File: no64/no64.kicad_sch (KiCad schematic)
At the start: 15 parts, among them J1 Analog Stick, SW10 Cup, SW11 Cright, SW12 Cdown, SW13 L, SW14 R, SW2 A, SW3 B, SW4 Dleft, SW5 Dup, SW6 Dright, SW7 Ddown, SW8 START, SW9 Cleft, U1 Pico

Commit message: More WIP
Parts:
- added C18: 10u, PhobGCC_2_0_0_footprints:C_0805_2012Metric, symbol Device:C
- added D1: D_Schottky, symbol Device:D_Schottky
- added J2: Conn_01x04_Socket, Connector_PinHeader_2.00mm:PinHeader_1x04_P2.00mm_Vertical, symbol Connector:Conn_01x04_Socket
- added P1: USB_C_Plug_USB2.0, symbol Connector:USB_C_Plug_USB2.0
- added U2: AMS1117-3.3, Package_TO_SOT_SMD:SOT-223-3_TabPin2, symbol Regulator_Linear:AMS1117-3.3
- J1: footprint (none) -> Connector_JST:JST_PH_S6B-PH-K_1x06_P2.00mm_Horizontal
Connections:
- net 3V3: no longer U1.36 (3V3)
- net A: now also U1.15 (GPIO11)
- net B: now also U1.14 (GPIO10)
- net Cdown: now also U1.20 (GPIO15)
- net Cleft: now also U1.16 (GPIO12)
- net Cright: now also U1.19 (GPIO14)
- net Cup: now also U1.17 (GPIO13)
- net GND: now also C18.2, J2.2 (Pin_2), U2.1 (GND)
- net L: now also U1.22 (GPIO17)
- net R: now also U1.21 (GPIO16)
- net START: now also U1.12 (GPIO9)
- net N64 +3V3: now reaches U1.39 (VSYS)
- net N64 +3V3: now also J2.4 (Pin_4)
- new net: D1.2 (A), U2.2 (VO)
- new net: P1.A4 (VBUS), P1.A9 (VBUS), P1.B4 (VBUS), P1.B9 (VBUS), U2.3 (VI)
- new net: P1.A1 (GND), P1.A12 (GND), P1.B1 (GND), P1.B12 (GND)
- new net +3V3: C18.1, D1.1 (K)
- new net JOY_DATA: J2.1 (Pin_1)
- new net PICO +3V3: U1.36 (3V3)
- no-connect marks 0 -> 1
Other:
- note added: "Controller to N64"
- note added: "JST-PH 2.0mm Pitch 6 Pin Female connector"
- note removed: "TODO: Analog stick should be a JST-PH 2.0mm Pitch 6 Pin Female connector"

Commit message: add button pads from phob (can almost all of of these), use better pico model
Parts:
- removed U1: Pico, RPi_Pico:RPi_Pico_SMD_TH, symbol MCU_RaspberryPi_and_Boards:Pico
- added A1: RaspberryPi_Pico, MCU_Module_RaspberryPi_Pico:RaspberryPi_Pico_Common_SMD, symbol MCU_Module_RaspberryPi_Pico:RaspberryPi_Pico
- added D2, D3: D_TVS, symbol Device:D_TVS
- added D5: CUS10S30,H3F, Diode_SMD:D_SOD-323, symbol Diode:MBR0520
- added H1, H2, H3, H8: 5.0mm, MountingHole:MountingHole_5mm, symbol Mechanical:MountingHole
- added H4, H5, H6, H7: 2.0mm, MountingHole:MountingHole_2mm, symbol Mechanical:MountingHole
- SW10, SW11, SW12, SW4, SW5, SW6, SW7, SW8, SW9: footprint (none) -> PhobGCC_2_0_0:Dpad_Contact_TL3315NF_2_ZigZag
- SW2, SW3: footprint (none) -> PhobGCC_2_0_0:ABXY_Contact_Omron_Switch_Circley
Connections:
- net A: now also A1.15 (GPIO11)
- net B: now also A1.14 (GPIO10)
- net Cdown: now also A1.20 (GPIO15)
- net Cleft: now also A1.16 (GPIO12)
- net Cright: now also A1.19 (GPIO14)
- net Cup: now also A1.17 (GPIO13)
- net GND: now also A1.13 (GND), A1.18 (GND), A1.23 (GND), A1.28 (GND), A1.3 (GND), A1.38 (GND), A1.8 (GND), D2.1 (A1), D3.1 (A1)
- net JOY_DATA: now also D2.2 (A2)
- net JOY_XA: now also A1.4 (GPIO2)
- net JOY_XB: now also A1.5 (GPIO3)
- net JOY_YA: now also A1.6 (GPIO4)
- net JOY_YB: now also A1.7 (GPIO5)
- net L: now also A1.21 (GPIO16)
- net N64 +3V3: now also D3.2 (A2), D5.2 (A)
- net PICO +3V3: now also A1.36 (3V3)
- net R: now also A1.22 (GPIO17)
- net START: now also A1.12 (GPIO9)
- new net: A1.39 (VSYS), D5.1 (K)
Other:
- note added: "Buttons"
- note added: "MCU"

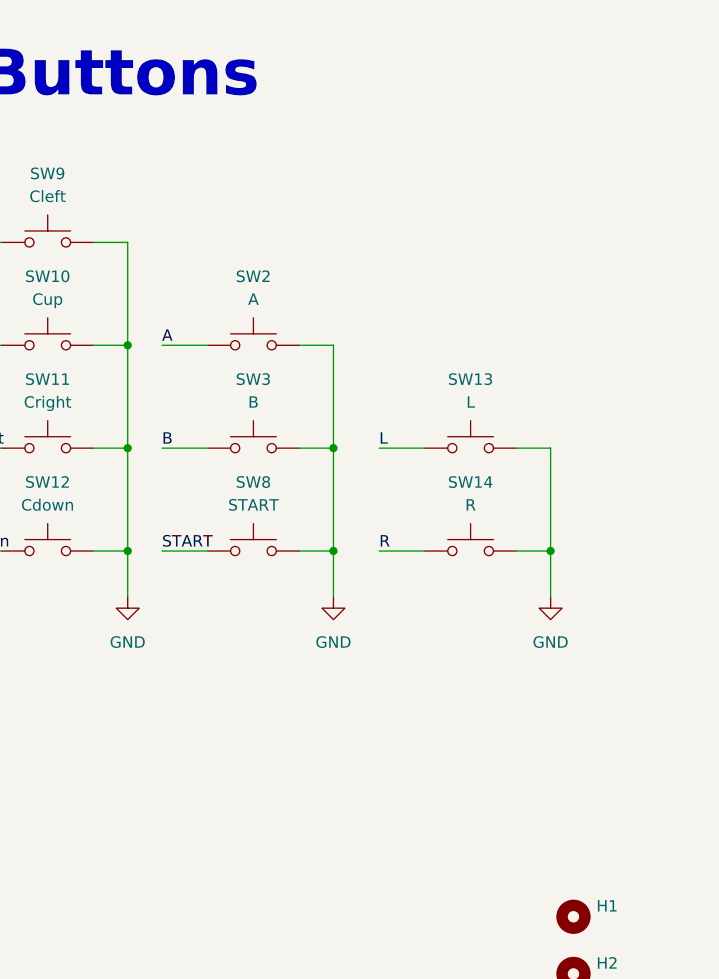
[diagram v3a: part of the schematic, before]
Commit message: Add pico 3d model, add L/R/START to PCB
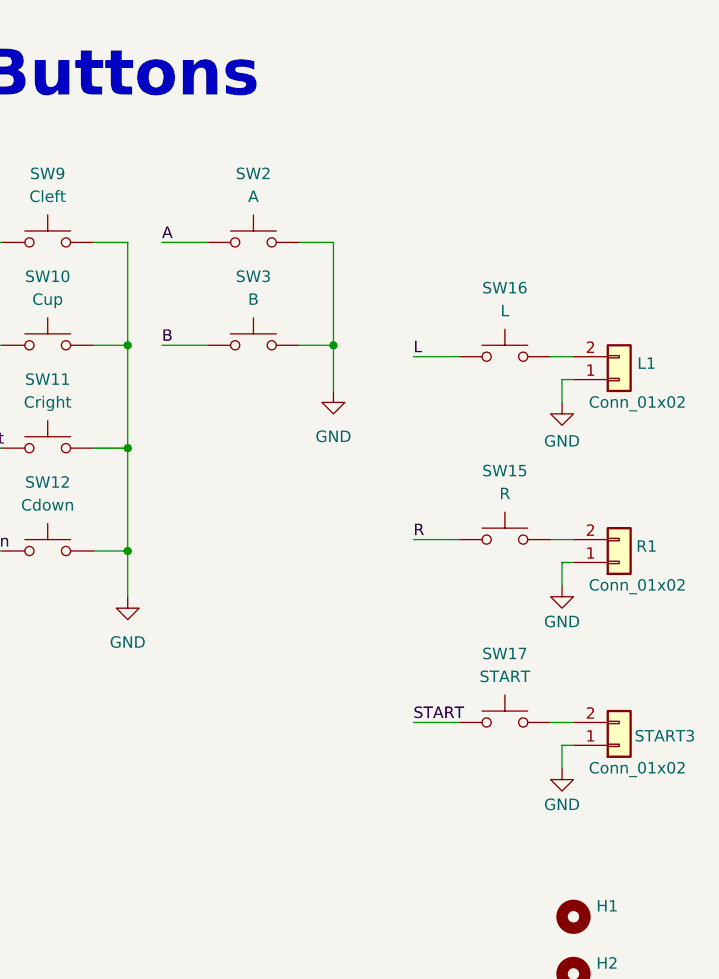
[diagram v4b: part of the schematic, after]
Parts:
- removed SW13: L, symbol Switch:SW_MEC_5G
- removed SW14: R, symbol Switch:SW_MEC_5G
- removed SW8: START, PhobGCC_2_0_0:Dpad_Contact_TL3315NF_2_ZigZag, symbol Switch:SW_MEC_5G
- added L1, R1, START3: Conn_01x02, Connector_PinSocket_2.00mm:PinSocket_1x02_P2.00mm_Vertical, symbol Connector_Generic:Conn_01x02
- added SW15: R, symbol Switch:SW_MEC_5G
- added SW16: L, symbol Switch:SW_MEC_5G
- added SW17: START, symbol Switch:SW_MEC_5G
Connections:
- net GND: now also L1.1 (Pin_1), R1.1 (Pin_1), START3.1 (Pin_1)
- net L: now also SW16.1 (A), SW16.2 (A)
- net R: now also SW15.1 (A), SW15.2 (A)
- net START: now also SW17.1 (A), SW17.2 (A)
- new net: R1.2 (Pin_2), SW15.3 (B), SW15.4 (B)
- new net: L1.2 (Pin_2), SW16.3 (B), SW16.4 (B)
- new net: START3.2 (Pin_2), SW17.3 (B), SW17.4 (B)
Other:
- moved on the sheet: SW2, SW3

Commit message: Rotate MCU, fix START/Z, misc cleanup
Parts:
- removed C18: 10u, PhobGCC_2_0_0_footprints:C_0805_2012Metric, symbol Device:C
- removed D1: D_Schottky, symbol Device:D_Schottky
- removed P1: USB_C_Plug_USB2.0, symbol Connector:USB_C_Plug_USB2.0
- removed U2: AMS1117-3.3, Package_TO_SOT_SMD:SOT-223-3_TabPin2, symbol Regulator_Linear:AMS1117-3.3
- added SW8: START, PhobGCC_2_0_0:Dpad_Contact_TL3315NF_2_ZigZag, symbol Switch:SW_MEC_5G
- SW17: value START -> Z
- SW2, SW3: footprint PhobGCC_2_0_0:ABXY_Contact_Omron_Switch_Circley -> PhobGCC_2_0_0:Dpad_Contact_TL3315NF_2_ZigZag
- renumbered START3 to Z3
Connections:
- net GND: now also SW8.3 (B), SW8.4 (B)
- net START: now also SW8.1 (A), SW8.2 (A); no longer SW17.1 (A), SW17.2 (A)
- net Z: now reaches A1.24 (GPIO18)
- net Z: now also SW17.1 (A), SW17.2 (A)
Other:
- moved on the sheet: D2, D3, J1, J2
